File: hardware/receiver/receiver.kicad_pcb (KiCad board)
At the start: 2 copper layers, 68.8 x 53.8 mm, 17 parts, among them J1 Input, J3 LED_B

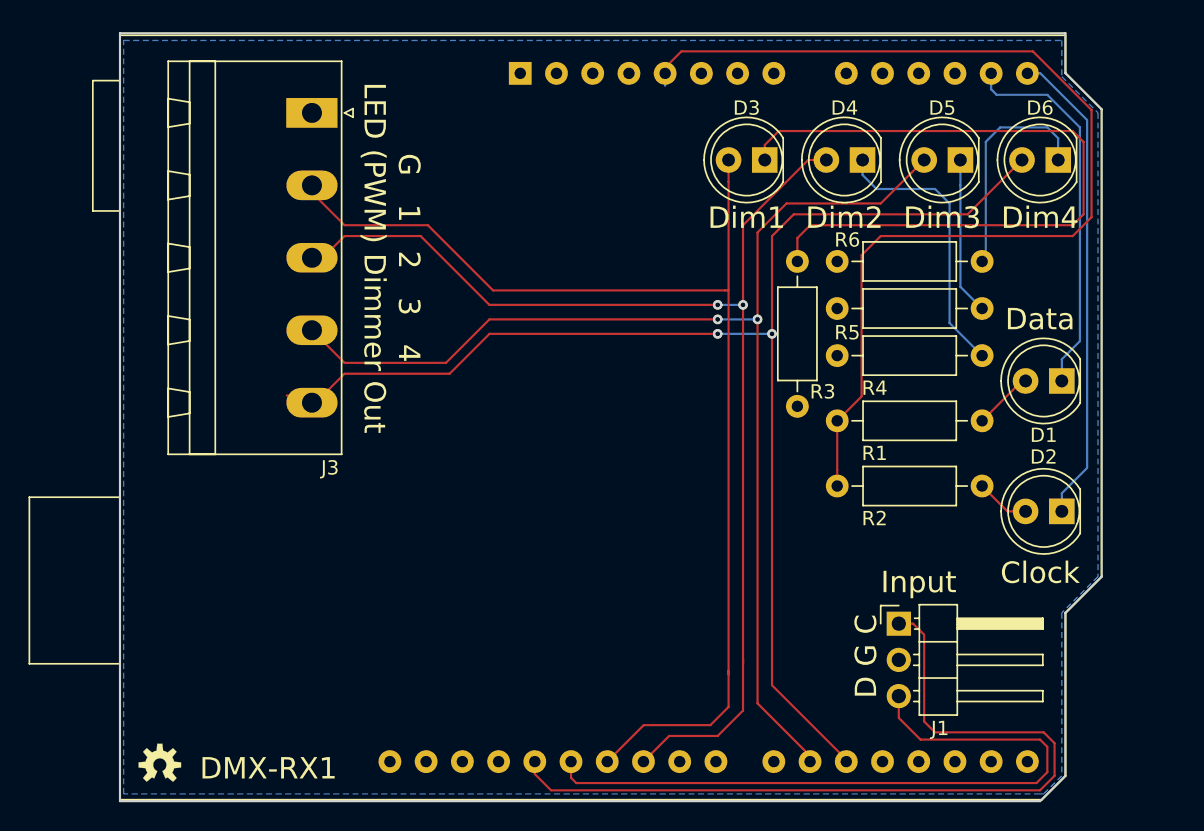
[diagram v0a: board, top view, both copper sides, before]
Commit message: Rev 1.1: - Fixed arduino shield footprint (it was backwards) - Added Fcu power plane - New Fcu layouts - Added rounded corners
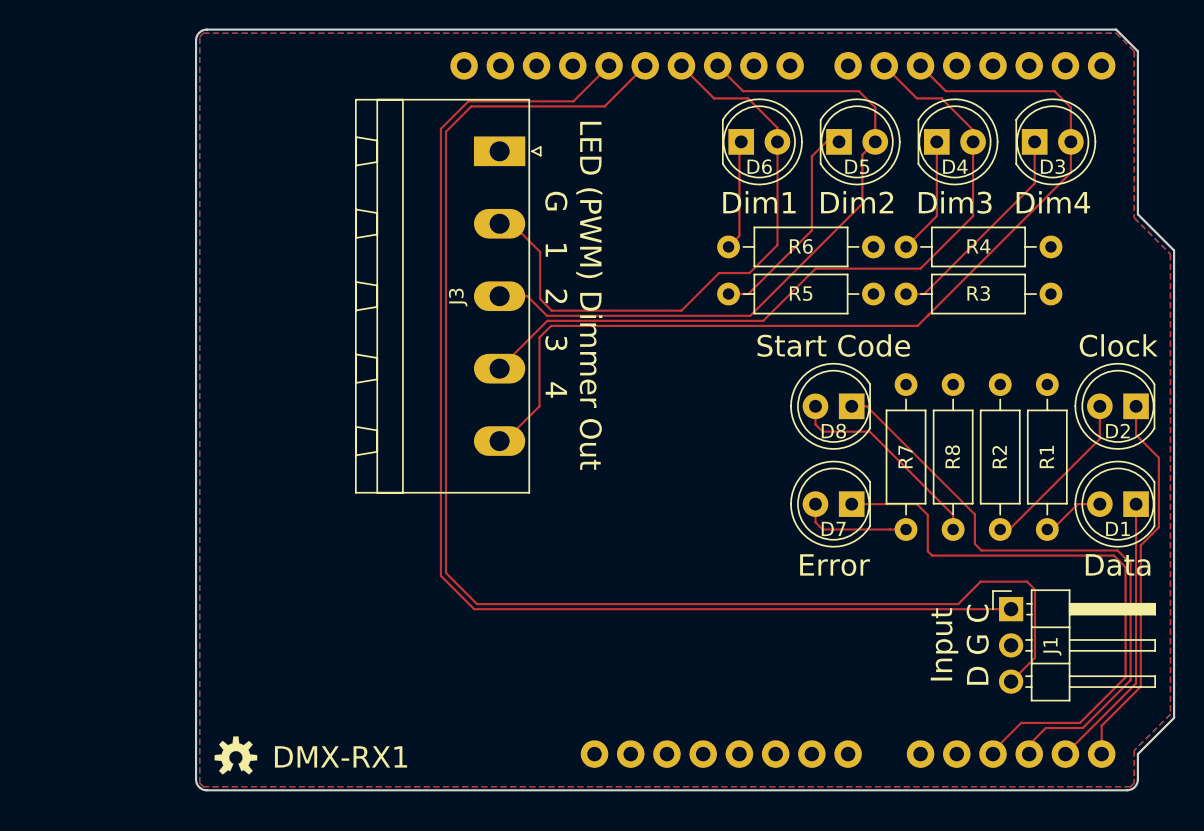
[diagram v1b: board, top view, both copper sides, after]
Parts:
- removed the ? at (113.8, 114.8)
- added ?: , footprints:OSHW-LOGO-S, F.Cu at (119.1, 114.3)
- added D7: ERROR, LED_THT:LED_D5.0mm, F.Cu at (162.3, 96.5)
- added D8: START_CODE, LED_THT:LED_D5.0mm, F.Cu at (162.3, 89.7)
- added R7: 330, Resistor_THT:R_Axial_DIN0207_L6.3mm_D2.5mm_P10.16mm_Horizontal, F.Cu at (166.1, 88.1)
- added R8: 330, Resistor_THT:R_Axial_DIN0207_L6.3mm_D2.5mm_P10.16mm_Horizontal, F.Cu at (169.4, 88.1)
- A1: footprint Module:Arduino_UNO_R3 -> footprints:ARDUINO_R3_NO_HOLES
- D3: value DIM0 -> DIM3
- D4: value DIM1 -> DIM2
- D5: value DIM2 -> DIM1
- D6: value DIM3 -> DIM0
- J3: value LED_B -> LED_OUT
- moved A1 26.3 mm to (150.6, 89.9)
- moved D6 22.3 mm to (154.6, 71.1), turned to 0 degrees
- moved R3 19.4 mm to (176.3, 81.8), turned to 180 degrees
- moved D3 19.0 mm to (175.1, 71.1), turned to 0 degrees
- moved R4 16.8 mm to (176.3, 78.5), turned to 180 degrees
- moved R1 14.9 mm to (176.0, 88.1), turned to 270 degrees
- moved R2 13.5 mm to (172.7, 88.1), turned to 270 degrees
- moved J3 13.4 mm to (137.6, 71.8)
- moved D1 10.1 mm to (182.2, 96.5)
- moved D2 9.02 mm to (182.2, 89.7)
- moved D5 8.60 mm to (161.4, 71.1), turned to 0 degrees
- moved J1 7.94 mm to (173.5, 103.9)
- moved G*** 5.92 mm to (120.1, 109.5)
- moved D4 5.36 mm to (168.3, 71.1), turned to 0 degrees
- moved R5 2.74 mm to (163.8, 81.8), turned to 180 degrees
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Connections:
- A1 pad 11: Net-(A1-Pad11) -> /~ERR
- A1 pad 12: Net-(A1-Pad12) -> /~SC
- D3 pad 2: /~DIM0 -> /~DIM3
- D4 pad 2: /~DIM1 -> /~DIM2
- D5 pad 2: /~DIM2 -> /~DIM1
- D6 pad 2: /~DIM3 -> /~DIM0
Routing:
- net +5V: track 75.0 -> 0.43 mm
- net /RX: track 49.6 -> 97.1 mm
- net /~SC: track 0.00 -> 43.2 mm
- net /~ERR: track 0.00 -> 41.9 mm
- net /~DIM0: track 81.5 -> 42.6 mm
- net Net-(D3-Pad1): track 51.6 -> 15.1 mm
- net /~DIM1: track 83.3 -> 48.6 mm, vias 2 -> 0
- net /~DIM2: track 86.4 -> 51.8 mm, vias 2 -> 0
- net /RXCLK: track 58.5 -> 87.2 mm
- net /~DIM3: track 94.0 -> 67.1 mm, vias 2 -> 0
- net Net-(D8-Pad2): track 0.00 -> 14.6 mm
- net Net-(D4-Pad1): track 19.6 -> 8.26 mm
- net Net-(D2-Pad2): track 3.78 -> 11.9 mm
- net Net-(D6-Pad1): track 15.8 -> 7.73 mm
- net Net-(D7-Pad2): track 0.00 -> 7.83 mm
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- added copper zone on F.Cu, net +5V
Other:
- board size 68.8 x 53.8 mm -> 68.6 x 53.3 mm
- net class Power added: clearance 0.1524, trace_width 0.3048, via_dia 1.27, via_drill 0.635
- board text added: "DMX-RX1, Rev 1.1 Crazy Giraffe Software"
- board text added: "Error"
- board text added: "LED (PWM) Dimmer Out G 1 2 3 4"
- board text added: "Start Code"
- board text removed: "DMX-RX1, Rev 1.0 Crazy Giraffe Software"
- board text removed: "G 1 2 3 4 LED (PWM) Dimmer Out"

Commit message: Users/sparky/txrx12 (#11)
* TX1 1.2, RX1 1.2
Move Clock LED to avoid ICSP connector.
Align TX Fast/Slo clock LEDS and RX start code/error LEDs.

* Add RXCLK to D9 connection for Leonardo PCINT5.

Co-authored-by: SparkyBobo <sparky@crazygiraffesoftware.com>
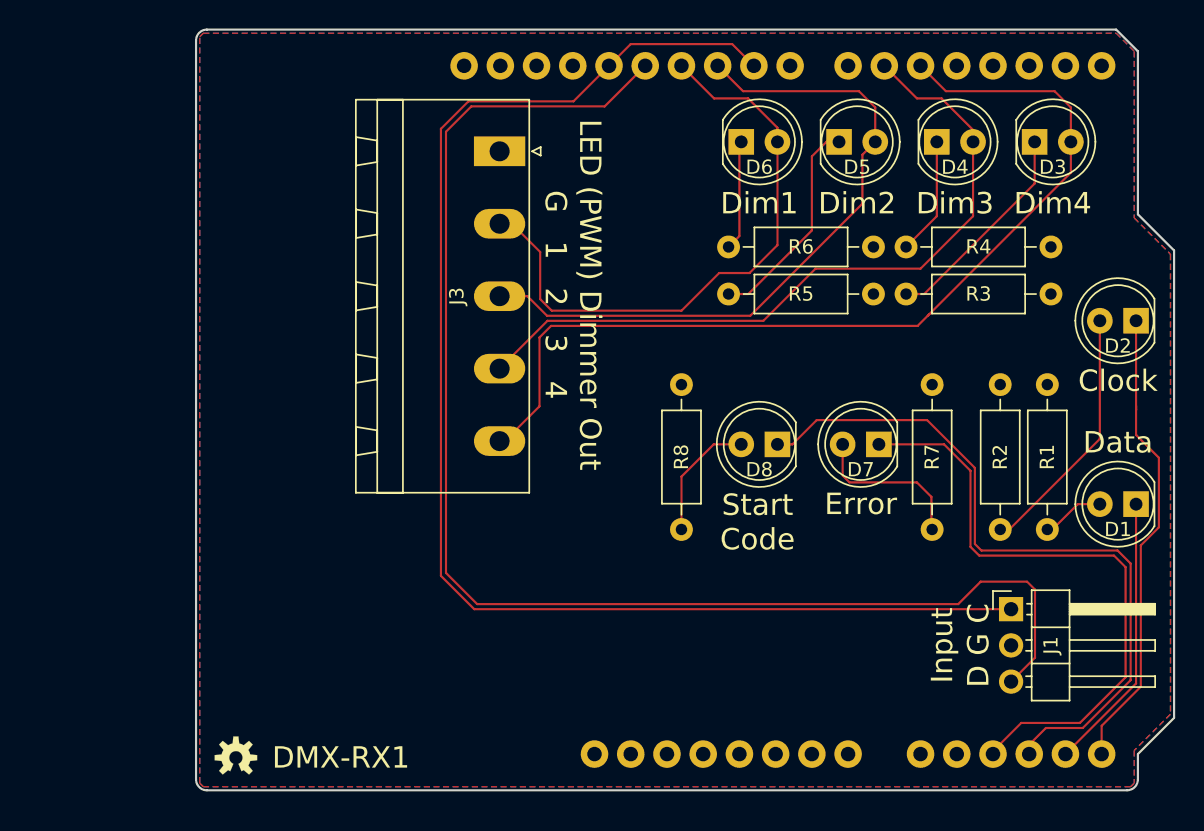
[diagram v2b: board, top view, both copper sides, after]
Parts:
- moved R8 19.1 mm to (150.4, 88.1)
- moved D2 6.00 mm to (182.2, 83.7)
- moved D8 5.85 mm to (157.1, 92.3)
- moved D7 4.60 mm to (164.2, 92.3)
- moved R7 1.83 mm to (167.9, 88.1)
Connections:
- A1 pad 24: Net-(A1-Pad24) -> /RXCLK
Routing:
- net /RXCLK: track 87.2 -> 98.7 mm
- net /~SC: track 43.2 -> 50.6 mm
- net /~CLOCK: track 26.7 -> 33.0 mm
- net Net-(D2-Pad2): track 11.9 -> 17.9 mm
- net Net-(D8-Pad2): track 14.6 -> 8.84 mm
- net Net-(D7-Pad2): track 7.83 -> 11.3 mm
- net /~ERR: track 41.9 -> 43.4 mm
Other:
- board text added: "DMX-RX1, Rev 1.2 Crazy Giraffe Software"
- board text removed: "DMX-RX1, Rev 1.1 Crazy Giraffe Software"

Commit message: Prototype version of DMX, Analog, and PWM IO Modules and both TX and RX IO interfaces.
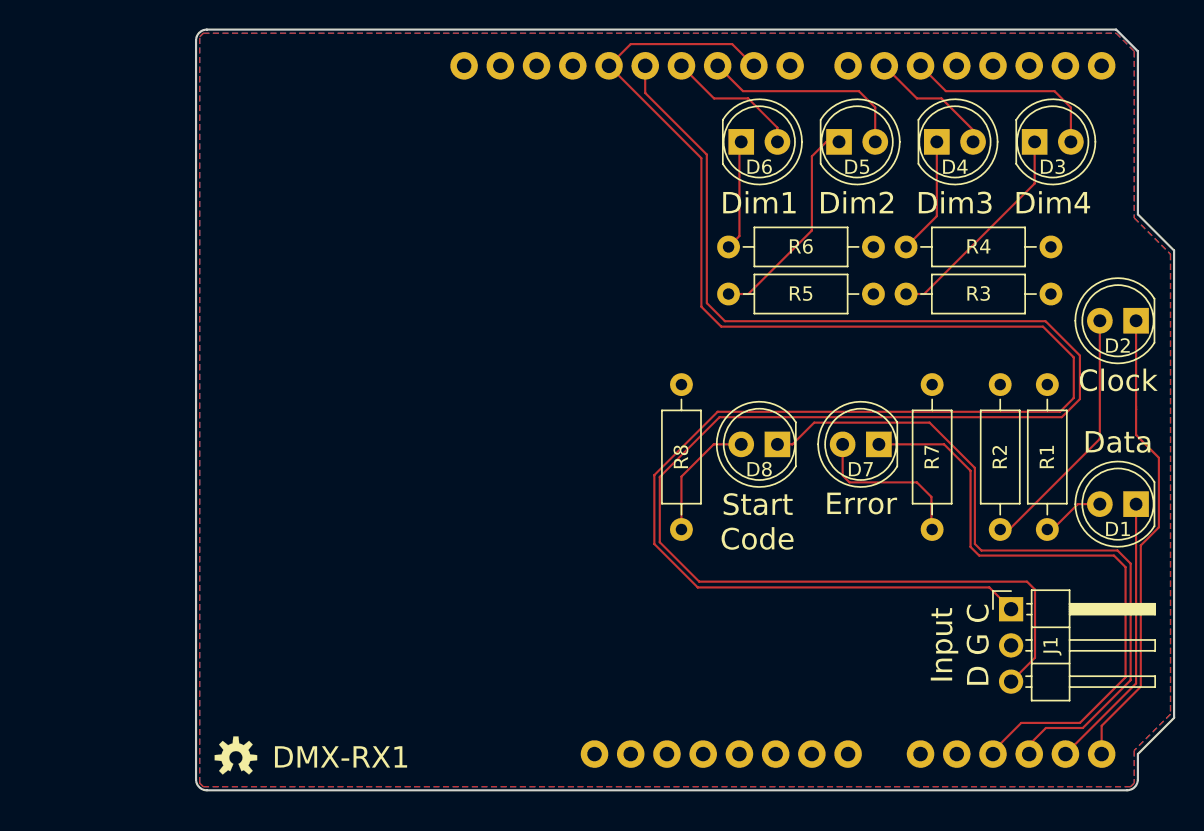
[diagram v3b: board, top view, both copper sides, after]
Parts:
- removed J3: LED_OUT, Connector_Phoenix_MSTB:PhoenixContact_MSTBA_2,5_5-G-5,08_1x05_P5.08mm_Horizontal
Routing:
- net /~DIM3: track 67.1 -> 14.2 mm
- net /~DIM2: track 51.8 -> 8.92 mm
- net /~DIM1: track 48.6 -> 14.7 mm
- net /~DIM0: track 42.6 -> 9.52 mm
- net /RXCLK: track 98.7 -> 126.2 mm
- net /RX: track 97.1 -> 120.3 mm
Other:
- board text added: "DMX-RX1, Rev 1.3 Crazy Giraffe Software"
- board text removed: "DMX-RX1, Rev 1.2 Crazy Giraffe Software"
- board text removed: "LED (PWM) Dimmer Out G 1 2 3 4"

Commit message: Rebrand to Sparky Bobo Designs
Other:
- board text added: "DMX-RX1, Rev 1.3 Sparky Bobo Designs"
- board text removed: "DMX-RX1, Rev 1.3 Crazy Giraffe Software"
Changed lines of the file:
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@@
     (date 2023-03-02)
     (rev 1.3)
-    (company "Crazy Giraffe Software")
+    (company "Sparky Bobo Designs")
     (comment 2 "Designed by: SparkyBobo")
     (comment 3 https://creativecommons.org/licenses/by-sa/4.0/)
@@
   (gr_line (start 180.848 63.246) (end 182.372 64.77) (layer Edge.Cuts) (width 0.15))
   (gr_line (start 117.094 63.246) (end 180.848 63.246) (layer Edge.Cuts) (width 0.15))
-  (gr_text "DMX-RX1, Rev 1.3\nCrazy Giraffe Software" (at 125.984 114.3) (layer B.SilkS)
+  (gr_text "DMX-RX1, Rev 1.3\nSparky Bobo Designs" (at 125.984 114.3) (layer B.SilkS)
     (effects (font (size 1 1) (thickness 0.15)) (justify mirror))
   )

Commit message: Library fixup. Rebrand.
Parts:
- added J2: PWM-34, Connector_PinHeader_2.54mm:PinHeader_1x03_P2.54mm_Horizontal, F.Cu at (142.5, 85.8)
- added J3: PWM_12, Connector_PinHeader_2.54mm:PinHeader_1x03_P2.54mm_Horizontal, F.Cu at (142.5, 76.1)
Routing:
- net /~DIM2: track 8.92 -> 51.9 mm
- net /~DIM3: track 14.2 -> 57.0 mm
- net /RXCLK: track 126.2 -> 87.3 mm, vias 0 -> 2
- net /RX: track 120.3 -> 85.0 mm, vias 0 -> 2
- net /~DIM0: track 9.52 -> 38.2 mm
- net /~DIM1: track 14.7 -> 43.3 mm
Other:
- board text added: "1 G 2"
- board text added: "3 G 4"
- board text added: "DMX-RX1, Rev 1.4 Sparky Bobo Designs"
- board text added: "PWM Outputs"
- board text removed: "DMX-RX1, Rev 1.3 Sparky Bobo Designs"

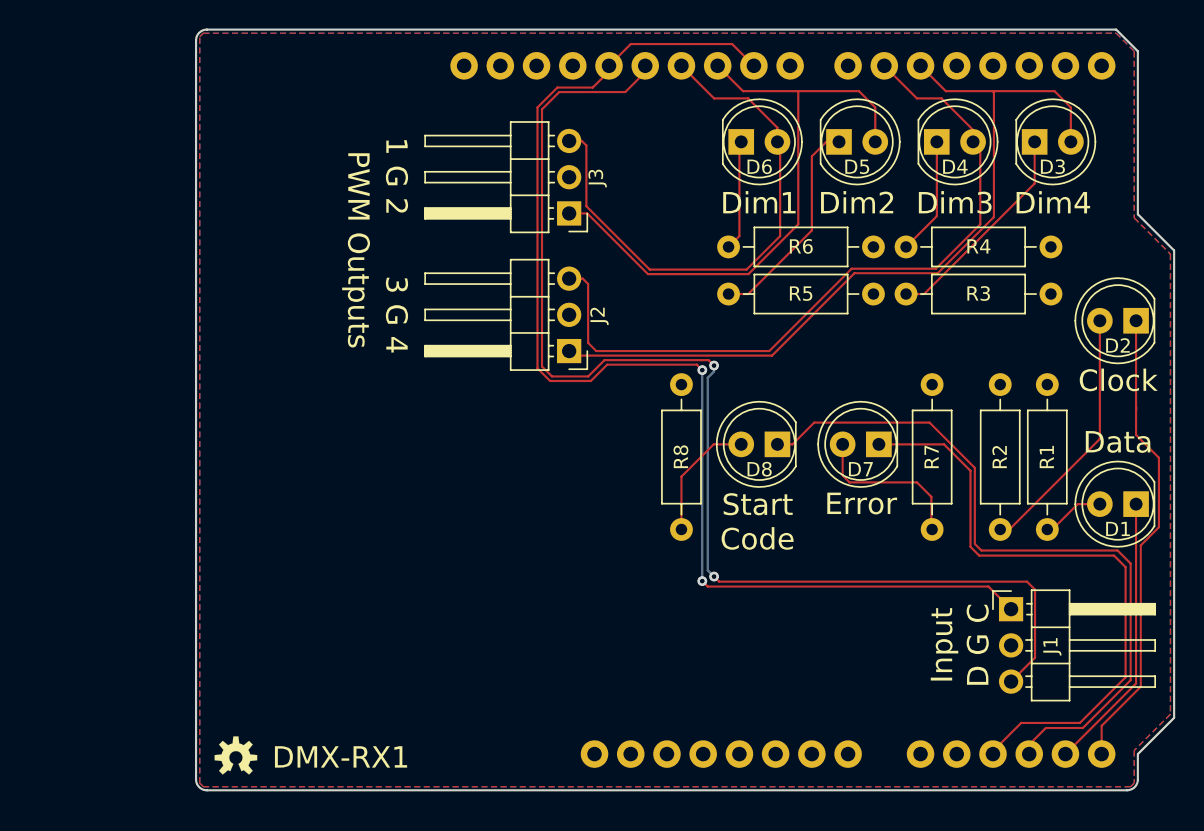
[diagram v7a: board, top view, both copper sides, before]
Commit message: Clean non-led files.
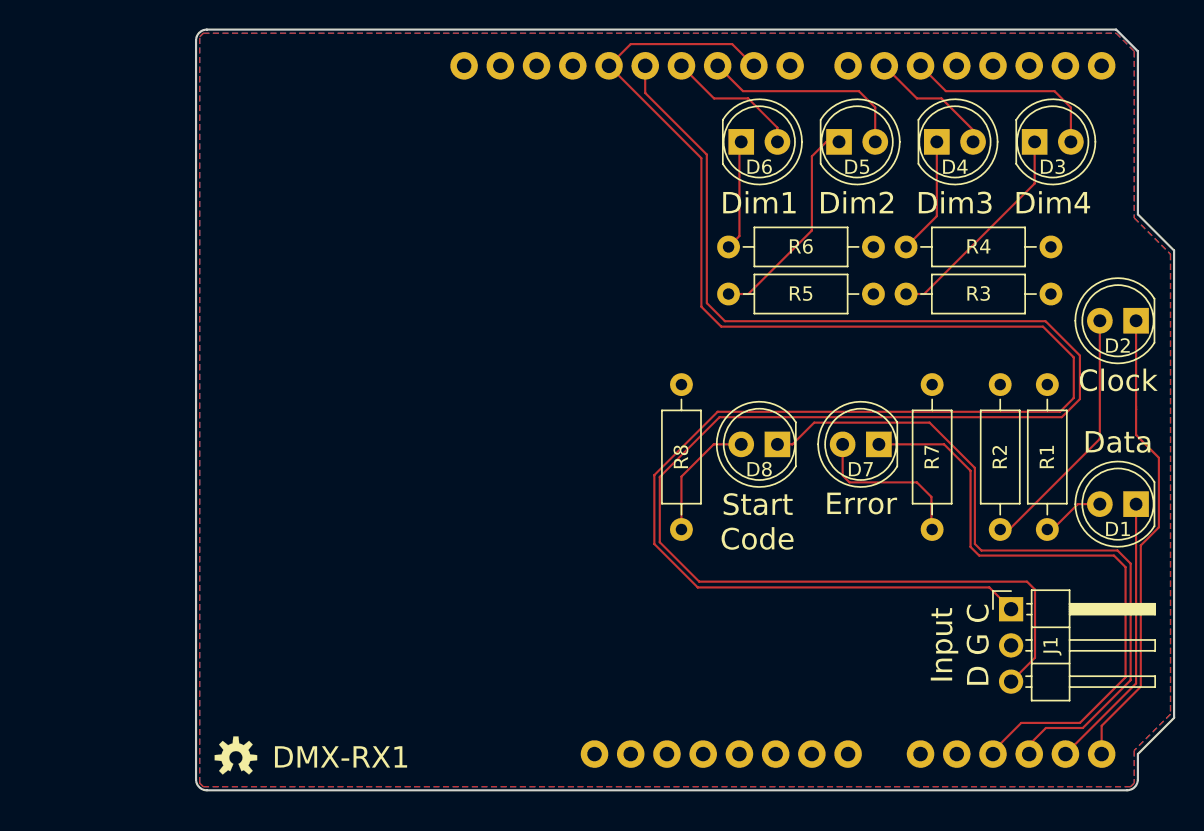
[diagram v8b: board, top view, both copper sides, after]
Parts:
- removed J2: PWM-34, Connector_PinHeader_2.54mm:PinHeader_1x03_P2.54mm_Horizontal
- removed J3: PWM_12, Connector_PinHeader_2.54mm:PinHeader_1x03_P2.54mm_Horizontal
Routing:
- net /~DIM2: track 51.9 -> 8.92 mm
- net /~DIM3: track 57.0 -> 14.2 mm
- net /RXCLK: track 87.3 -> 126.2 mm, vias 2 -> 0
- net /RX: track 85.0 -> 120.3 mm, vias 2 -> 0
- net /~DIM0: track 38.2 -> 9.52 mm
- net /~DIM1: track 43.3 -> 14.7 mm
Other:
- board text added: "DMX-RX1, Rev 1.3 Sparky Bobo Designs"
- board text removed: "1 G 2"
- board text removed: "3 G 4"
- board text removed: "DMX-RX1, Rev 1.4 Sparky Bobo Designs"
- board text removed: "PWM Outputs"
